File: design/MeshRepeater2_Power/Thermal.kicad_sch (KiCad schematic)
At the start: 24 parts, among them Q4 AO3401A, Q5 BSS138, Q6 AO3401A, Q7 AO3401A, U10 LM393XK, U11 LM285Z-2.5G

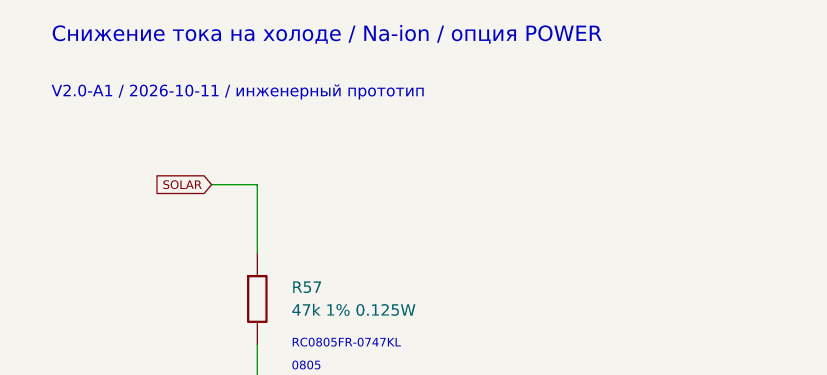
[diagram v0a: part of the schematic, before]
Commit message: Publish Mesh Repeater 2.0 A2
Add INA219 battery measurement with a 0.1 ohm shunt and vertical
12-pin interconnects through the middle shield. Publish updated
POWER, LOGIC and SHIELD KiCad sources, local models, BOM and A2
documentation with the completed routing and ground-via audit.

Preserve the V1 baseline and archives inside the V2 branch.
Validation: independent review 132/132; final artifact gate 499/499.
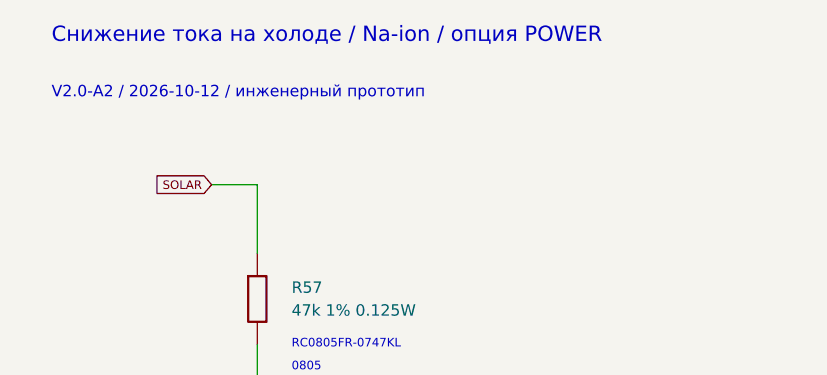
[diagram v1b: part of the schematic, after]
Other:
- note added: "V2.0-A2 / 2026-10-12 / инженерный прототип"
- note removed: "V2.0-A1 / 2026-10-11 / инженерный прототип"
